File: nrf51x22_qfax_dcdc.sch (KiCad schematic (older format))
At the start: 19 parts, among them U1 nrf51822-qfax, X1 Crystal

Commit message: add vias to footprint and swap in
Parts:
- U1: footprint nrf:nrf51-qfax -> nrf:nrf51-qfax-1ep-vias
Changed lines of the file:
@@
 F 0 "U1" H 2950 4250 60  0000 C CNN
 F 1 "nrf51822-qfax" H 2950 4400 60  0000 C CNN
-F 2 "nrf:nrf51-qfax" H 2900 4650 60  0001 C CNN
+F 2 "nrf:nrf51-qfax-1ep-vias" H 2900 4650 60  0001 C CNN
 F 3 "" H 2900 4650 60  0000 C CNN
 	1    3000 4300

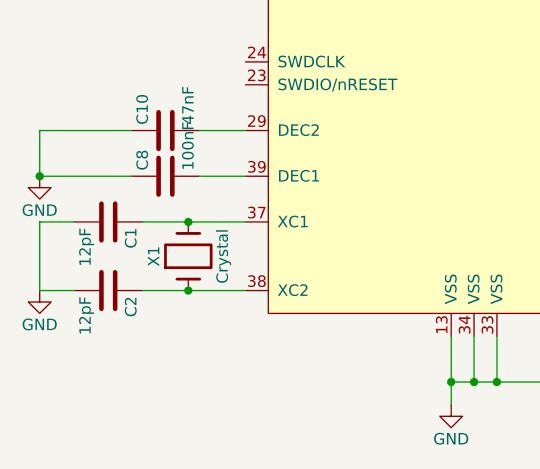
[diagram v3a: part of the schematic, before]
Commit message: fix crystal component so hooks grounds to GND, gerbers
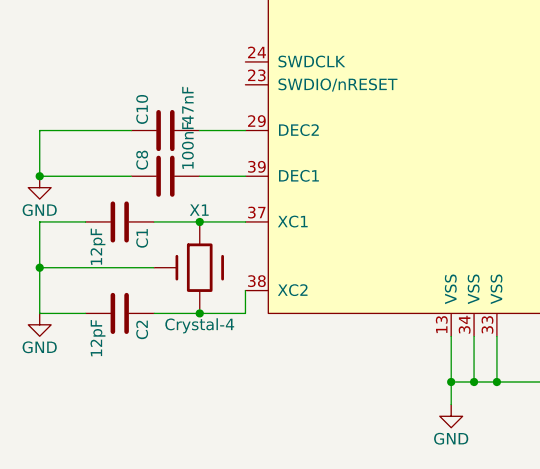
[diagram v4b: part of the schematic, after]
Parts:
- removed X1: Crystal, dcdc:BT-XTAL_2520, symbol Crystal
- added X1: Crystal-4, dcdc:BT-XTAL_2520, symbol Crystal-4
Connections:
- net GND: now also X1.2 (4), X1.4
- net at C2.1, U1.38 (XC2): now also X1.1
- net at C1.1, U1.37 (XC1): now also X1.3
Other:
- moved on the sheet: C1, C2
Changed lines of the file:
@@
 L C C2
 U 1 1 566CD1BB
-P 1200 5800
-F 0 "C2" H 1225 5900 50  0000 L CNN
-F 1 "12pF" H 1225 5700 50  0000 L CNN
-F 2 "dcdc:CAPC1005X04L" H 1238 5650 50  0001 C CNN
-F 3 "" H 1200 5800 50  0000 C CNN
-	1    1200 5800
+P 1250 5900
+F 0 "C2" H 1275 6000 50  0000 L CNN
+F 1 "12pF" H 1275 5800 50  0000 L CNN
+F 2 "dcdc:CAPC1005X04L" H 1288 5750 50  0001 C CNN
+F 3 "" H 1250 5900 50  0000 C CNN
+	1    1250 5900
 	0    1    1    0
 $EndComp
@@
 L C C1
 U 1 1 566CD21B
-P 1200 5500
-F 0 "C1" H 1225 5600 50  0000 L CNN
-F 1 "12pF" H 1225 5400 50  0000 L CNN
-F 2 "dcdc:CAPC1005X04L" H 1238 5350 50  0001 C CNN
-F 3 "" H 1200 5500 50  0000 C CNN
-	1    1200 5500
+P 1250 5500
+F 0 "C1" H 1275 5600 50  0000 L CNN
+F 1 "12pF" H 1275 5400 50  0000 L CNN
+F 2 "dcdc:CAPC1005X04L" H 1288 5350 50  0001 C CNN
+F 3 "" H 1250 5500 50  0000 C CNN
+	1    1250 5500
 	0    1    1    0
 $EndComp
@@
 L GND #PWR05
 U 1 1 566CD572
-P 900 5800
-F 0 "#PWR05" H 900 5550 50  0001 C CNN
-F 1 "GND" H 900 5650 50  0000 C CNN
-F 2 "" H 900 5800 50  0000 C CNN
-F 3 "" H 900 5800 50  0000 C CNN
-	1    900  5800
-	1    0    0    -1
-$EndComp
-Connection ~ 2700 6200
-Wire Wire Line
-	2700 6200 3400 6200
-Connection ~ 2800 6200
-Wire Wire Line
-	1350 5500 1800 5500
-Wire Wire Line
-	1350 5800 1800 5800
-Wire Wire Line
-	4200 2800 5100 2800
-Wire Wire Line
-	3700 2100 3700 2300
-Wire Wire Line
-	3500 2500 3500 2600
-Wire Wire Line
-	3700 2600 3700 2500
-Wire Wire Line
-	3300 2600 3300 2500
-Wire Wire Line
-	3300 2500 3500 2500
-Wire Wire Line
-	3400 1700 3400 2500
-Connection ~ 3400 2500
-Wire Wire Line
-	4400 1700 4400 1900
-Wire Wire Line
-	4100 1700 4100 1900
-Wire Wire Line
-	3400 6200 3400 6000
-Connection ~ 2900 6200
-Connection ~ 1550 5500
-Connection ~ 1550 5800
-Wire Wire Line
-	1050 5800 900  5800
-Wire Wire Line
-	1050 5500 900  5500
-Wire Wire Line
-	900  5500 900  5800
-Wire Wire Line
-	2300 2600 2300 2500
-Wire Wire Line
-	2300 2500 2500 2500
-Wire Wire Line
-	2500 2500 2500 2600
-Wire Wire Line
-	2400 1700 2400 2500
-Connection ~ 2400 2500
-Wire Wire Line
-	2000 2200 2000 2300
-Wire Wire Line
-	2000 2300 2200 2300
-Wire Wire Line
-	4100 2200 4100 2300
-Wire Wire Line
-	4400 2200 4400 2300
+P 900 5900
+F 0 "#PWR05" H 900 5650 50  0001 C CNN
+F 1 "GND" H 900 5750 50  0000 C CNN
+F 2 "" H 900 5900 50  0000 C CNN
+F 3 "" H 900 5900 50  0000 C CNN
+	1    900  5900
+	1    0    0    -1
+$EndComp
 $Comp
 L GND #PWR06
@@
 	1    0    0    -1
 $EndComp
-Wire Wire Line
-	900  5300 1300 5300
-Wire Wire Line
-	900  5100 1300 5100
-Wire Wire Line
-	4800 3000 4800 3100
-Wire Wire Line
-	4800 3300 4800 3400
-Wire Wire Line
-	5400 2800 5800 2800
-Connection ~ 5600 2800
-Wire Wire Line
-	6000 2800 6200 2800
 $Comp
 L GND #PWR07
@@
 	1    0    0    -1
 $EndComp
-Connection ~ 4800 2800
-Wire Wire Line
-	4200 2900 4700 2900
-Wire Wire Line
-	4700 2900 4700 3000
-Wire Wire Line
-	4700 3000 4800 3000
-Wire Wire Line
-	4800 3400 4600 3400
-Wire Wire Line
-	4600 3400 4600 3000
-Wire Wire Line
-	4600 3000 4200 3000
-Connection ~ 4800 3400
-Connection ~ 4800 3000
-Wire Wire Line
-	1800 5100 1600 5100
-Wire Wire Line
-	1800 5300 1600 5300
-Wire Wire Line
-	900  5300 900  5100
-Connection ~ 900  5300
-Connection ~ 4100 1700
-Wire Wire Line
-	3400 1700 4400 1700
-Wire Wire Line
-	2000 1700 2400 1700
-Wire Wire Line
-	2000 1900 2000 1700
-Connection ~ 2000 1700
-Wire Wire Line
-	2200 1900 2200 1700
-Connection ~ 2200 1700
-Wire Wire Line
-	2200 2300 2200 2200
-Connection ~ 2000 2300
-Wire Wire Line
-	3700 1700 3700 1900
-Connection ~ 3700 1700
 Text Label 2000 1600 0    60   ~ 0
 VCC_nRF
-$Comp
-L Crystal X1
-U 1 1 566BCA38
-P 1550 5650
-F 0 "X1" H 1550 5800 50  0000 C CNN
-F 1 "Crystal" H 1550 5500 50  0000 C CNN
-F 2 "dcdc:BT-XTAL_2520" H 1550 5650 50  0001 C CNN
-F 3 "" H 1550 5650 50  0000 C CNN
-	1    1550 5650
-	0    -1   -1   0
-$EndComp
-Wire Wire Line
-	2800 6000 2800 6200
-Wire Wire Line
-	2900 6200 2900 6000
-Wire Wire Line
-	2700 6000 2700 6300
 $Comp
 L nrf51822-qfax U1
@@
 	1    0    0    -1
 $EndComp
+Connection ~ 2700 6200
+Wire Wire Line
+	2700 6200 3400 6200
+Connection ~ 2800 6200
+Wire Wire Line
+	4200 2800 5100 2800
+Wire Wire Line
+	3700 2100 3700 2300
+Wire Wire Line
+	3500 2500 3500 2600
+Wire Wire Line
+	3700 2600 3700 2500
+Wire Wire Line
+	3300 2600 3300 2500
+Wire Wire Line
+	3300 2500 3500 2500
+Wire Wire Line
+	3400 1700 3400 2500
+Connection ~ 3400 2500
+Wire Wire Line
+	4400 1700 4400 1900
+Wire Wire Line
+	4100 1700 4100 1900
+Wire Wire Line
+	3400 6200 3400 6000
+Connection ~ 2900 6200
+Wire Wire Line
+	900  5500 900  5900
+Wire Wire Line
+	2300 2600 2300 2500
+Wire Wire Line
+	2300 2500 2500 2500
+Wire Wire Line
+	2500 2500 2500 2600
+Wire Wire Line
+	2400 1700 2400 2500
+Connection ~ 2400 2500
+Wire Wire Line
+	2000 2200 2000 2300
+Wire Wire Line
+	2000 2300 2200 2300
+Wire Wire Line
+	4100 2200 4100 2300
+Wire Wire Line
+	4400 2200 4400 2300
+Wire Wire Line
+	900  5300 1300 5300
+Wire Wire Line
+	900  5100 1300 5100
+Wire Wire Line
+	4800 3000 4800 3100
+Wire Wire Line
+	4800 3300 4800 3400
+Wire Wire Line
+	5400 2800 5800 2800
+Connection ~ 5600 2800
+Wire Wire Line
+	6000 2800 6200 2800
+Connection ~ 4800 2800
+Wire Wire Line
+	4200 2900 4700 2900
+Wire Wire Line
+	4700 2900 4700 3000
+Wire Wire Line
+	4700 3000 4800 3000
+Wire Wire Line
+	4800 3400 4600 3400
+Wire Wire Line
+	4600 3400 4600 3000
+Wire Wire Line
+	4600 3000 4200 3000
+Connection ~ 4800 3400
+Connection ~ 4800 3000
+Wire Wire Line
+	1800 5100 1600 5100
+Wire Wire Line
+	1800 5300 1600 5300
+Wire Wire Line
+	900  5300 900  5100
+Connection ~ 900  5300
+Connection ~ 4100 1700
+Wire Wire Line
+	3400 1700 4400 1700
+Wire Wire Line
+	2000 1700 2400 1700
+Wire Wire Line
+	2000 1900 2000 1700
+Connection ~ 2000 1700
+Wire Wire Line
+	2200 1900 2200 1700
+Connection ~ 2200 1700
+Wire Wire Line
+	2200 2300 2200 2200
+Connection ~ 2000 2300
+Wire Wire Line
+	3700 1700 3700 1900
+Connection ~ 3700 1700
+Wire Wire Line
+	2800 6000 2800 6200
+Wire Wire Line
+	2900 6200 2900 6000
+Wire Wire Line
+	2700 6000 2700 6300
+Connection ~ 1600 5900
+Wire Wire Line
+	1800 5900 1800 5800
+Wire Wire Line
+	1400 5900 1800 5900
+Wire Wire Line
+	1100 5500 900  5500
+Wire Wire Line
+	900  5900 1100 5900
+Wire Wire Line
+	1400 5700 900  5700
+Connection ~ 900  5700
+Wire Wire Line
+	1400 5500 1800 5500
+Connection ~ 1600 5500
+$Comp
+L Crystal-4 X1
+U 1 1 56D1F3A1
+P 1600 5700
+F 0 "X1" H 1600 5950 50  0000 C CNN
+F 1 "Crystal-4" H 1600 5450 50  0000 C CNN
+F 2 "dcdc:BT-XTAL_2520" H 1600 5700 50  0001 C CNN
+F 3 "" H 1600 5700 50  0000 C CNN
+	1    1600 5700
+	1    0    0    -1
+$EndComp

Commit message: fix missing low freq crystal on schematic
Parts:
- added C13, C14: 12pF, dcdc:CAPC1005X04L, symbol C
- added X2: 32.768kHz, dcdc:XTAL_3215, symbol Crystal_Small
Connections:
- net GND: now also C13.1, C14.1
- net at U1.45 (P0.26): now also C13.2, X2.1
- net at U1.46 (P0.27): now also C14.2, X2.2
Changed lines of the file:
@@
 	1    0    0    -1
 $EndComp
+$Comp
+L C C13
+U 1 1 56D1F8D7
+P 4850 5300
+F 0 "C13" H 4875 5400 50  0000 L CNN
+F 1 "12pF" H 4875 5200 50  0000 L CNN
+F 2 "dcdc:CAPC1005X04L" H 4888 5150 50  0001 C CNN
+F 3 "" H 4850 5300 50  0000 C CNN
+	1    4850 5300
+	0    1    1    0
+$EndComp
+$Comp
+L C C14
+U 1 1 56D1F931
+P 4850 5500
+F 0 "C14" H 4875 5600 50  0000 L CNN
+F 1 "12pF" H 4875 5400 50  0000 L CNN
+F 2 "dcdc:CAPC1005X04L" H 4888 5350 50  0001 C CNN
+F 3 "" H 4850 5500 50  0000 C CNN
+	1    4850 5500
+	0    1    1    0
+$EndComp
+$Comp
+L Crystal_Small X2
+U 1 1 56D1F980
+P 4500 5400
+F 0 "X2" H 4500 5500 50  0000 C CNN
+F 1 "32.768kHz" H 4500 5300 50  0000 C CNN
+F 2 "dcdc:XTAL_3215" H 4500 5400 50  0001 C CNN
+F 3 "" H 4500 5400 50  0000 C CNN
+	1    4500 5400
+	0    1    1    0
+$EndComp
+Wire Wire Line
+	4200 5300 4700 5300
+Connection ~ 4500 5300
+Connection ~ 4500 5500
+Wire Wire Line
+	5000 5500 5100 5500
+Wire Wire Line
+	5100 5300 5100 5600
+Wire Wire Line
+	5100 5300 5000 5300
+$Comp
+L GND #PWR010
+U 1 1 56D20387
+P 5100 5600
+F 0 "#PWR010" H 5100 5350 50  0001 C CNN
+F 1 "GND" H 5100 5450 50  0000 C CNN
+F 2 "" H 5100 5600 50  0000 C CNN
+F 3 "" H 5100 5600 50  0000 C CNN
+	1    5100 5600
+	1    0    0    -1
+$EndComp
+Connection ~ 5100 5500
+Wire Wire Line
+	4200 5400 4300 5400
+Wire Wire Line
+	4300 5400 4300 5500
+Wire Wire Line
+	4300 5500 4700 5500
 $EndSCHEMATC

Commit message: fill in component fields for bom
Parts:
- C1, C13, C14, C2: Description (none) -> Capacitor NP0 ±2%; Distributor 1 (none) -> 490-6197-1-ND; Manufacturer (none) -> Yageo; Manufacturer Part (none) -> GRM1555C1H120GA01D
- C10: Description (none) -> Capacitor X7R ±10%; Distributor 1 (none) -> 311-1717-1-ND; Manufacturer (none) -> Yageo; Manufacturer Part (none) -> CC0402KRX7R8BB473
- C11: Description (none) -> Capacitor X7R ±10%; Distrubutor 1 (none) -> 311-1345-1-ND; Manufacturer (none) -> Yageo; Manufacturer Part (none) -> CC0402KRX7R6BB104
- C12: Description (none) -> Capacitor X7R ±10%; Distributor 1 (none) -> 311-1446-1-ND; Manufacturer (none) -> Yageo; Manufacturer Part (none) -> CC0603KRX7R7BB105
- C3: Description (none) -> Capacitor X7R ±10%; Distributor 1 (none) -> 311-1037-1-ND; Manufacturer (none) -> Yageo; Manufacturer Part (none) -> CC0402KRX7R9BB222
- C4, C5, C6: Description (none) -> Capacitor NP0 ±0.1pF
- C7: Description (none) -> Capacitor X5R ±10%; Distributor 1 (none) -> 490-10730-1-ND; Manufacturer (none) -> Murata Electronics North America; Manufacturer Part (none) -> GRM188R61C475KE11D
- C8: Description (none) -> Capacitor X7R ±10%; Distributor 1 (none) -> 311-1345-1-ND; Manufacturer (none) -> Yageo; Manufacturer Part (none) -> CC0402KRX7R6BB104
- C9: Description (none) -> Capacitor X7R ±10%; Distributor 1 (none) -> 311-1036-1-ND; Manufacturer (none) -> Yageo; Manufacturer Part (none) -> CC0402KRX7R9BB102
- L1, L2, L3: Description (none) -> High frequency chip inductor ±5%
- L4: Description (none) -> Chip inductor IDC min = 50 mA ±20%; Distributor 1 (none) -> 445-6755-1-ND; Manufacturer (none) -> TDK; Manufacturer Part (none) -> MLZ1608N100LT000
- L5: Description (none) -> High frequency chip inductor ±10%; Distributor 1 (none) -> 445-1469-1-ND; Manufacturer (none) -> TDK; Manufacturer Part (none) -> MLK1005S15NJT000
- U1: Manufacturer (none) -> Nordic Semiconductor ASA; Manufacturer Part (none) -> NRF51822-QFAC-T
- X1: Description (none) -> 8pF ±40ppm; Distributor 1 (none) -> 644-1169-1-ND; Manufacturer (none) -> NDK; Manufacturer Part (none) -> NX2520SA-16MHZ-STD-CSW-5
- X2: Description (none) -> 9pF ±20ppm; Distributor 1 (none) -> 535-9544-1-ND; Manufacturer (none) -> Abracon LLC; Manufacturer Part (none) -> ABS07-32.768KHZ-9-T
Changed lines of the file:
@@
 F 2 "dcdc:INDC1005X04L" H 3700 2000 50  0001 C CNN
 F 3 "" H 3700 2000 50  0000 C CNN
+F 4 "High frequency chip inductor ±10%" H 3700 2000 60  0001 C CNN "Description"
+F 5 "MLK1005S15NJT000" H 3700 2000 60  0001 C CNN "Manufacturer Part"
+F 6 "TDK" H 3700 2000 60  0001 C CNN "Manufacturer"
+F 7 "445-1469-1-ND" H 3700 2000 60  0001 C CNN "Distributor 1"
 	1    3700 2000
 	1    0    0    -1
@@
 F 2 "dcdc:INDC1608X06L" H 3700 2400 50  0001 C CNN
 F 3 "" H 3700 2400 50  0000 C CNN
+F 4 "Chip inductor IDC min = 50 mA ±20%" H 3700 2400 60  0001 C CNN "Description"
+F 5 "MLZ1608N100LT000" H 3700 2400 60  0001 C CNN "Manufacturer Part"
+F 6 "TDK" H 3700 2400 60  0001 C CNN "Manufacturer"
+F 7 "445-6755-1-ND" H 3700 2400 60  0001 C CNN "Distributor 1"
 	1    3700 2400
 	1    0    0    -1
@@
 F 2 "dcdc:CAPC1608X06L" H 4438 1900 50  0001 C CNN
 F 3 "" H 4400 2050 50  0000 C CNN
+F 4 "Capacitor X7R ±10%" H 4400 2050 60  0001 C CNN "Description"
+F 5 "CC0603KRX7R7BB105" H 4400 2050 60  0001 C CNN "Manufacturer Part"
+F 6 "Yageo" H 4400 2050 60  0001 C CNN "Manufacturer"
+F 7 "311-1446-1-ND" H 4400 2050 60  0001 C CNN "Distributor 1"
 	1    4400 2050
 	1    0    0    -1
@@
 F 2 "dcdc:CAPC1005X04L" H 4138 1900 50  0001 C CNN
 F 3 "" H 4100 2050 50  0000 C CNN
+F 4 "Capacitor X7R ±10%" H 4100 2050 60  0001 C CNN "Description"
+F 5 "CC0402KRX7R9BB102" H 4100 2050 60  0001 C CNN "Manufacturer Part"
+F 6 "Yageo" H 4100 2050 60  0001 C CNN "Manufacturer"
+F 7 "311-1036-1-ND" H 4100 2050 60  0001 C CNN "Distributor 1"
 	1    4100 2050
 	1    0    0    -1
@@
 F 2 "dcdc:INDC1005X04L" H 4800 3200 50  0001 C CNN
 F 3 "" H 4800 3200 50  0000 C CNN
+F 4 "High frequency chip inductor ±5%" H 4800 3200 60  0001 C CNN "Description"
 	1    4800 3200
 	1    0    0    -1
@@
 F 2 "dcdc:INDC1005X04L" H 4800 2900 50  0001 C CNN
 F 3 "" H 4800 2900 50  0000 C CNN
+F 4 "High frequency chip inductor ±5%" H 4800 2900 60  0001 C CNN "Description"
 	1    4800 2900
 	1    0    0    -1
@@
 F 2 "dcdc:INDC1005X04L" H 5900 2800 50  0001 C CNN
 F 3 "" H 5900 2800 50  0000 C CNN
+F 4 "High frequency chip inductor ±5%" H 5900 2800 60  0001 C CNN "Description"
 	1    5900 2800
 	0    -1   -1   0
@@
 F 2 "dcdc:CAPC1005X04L" H 4838 3400 50  0001 C CNN
 F 3 "" H 4800 3550 50  0000 C CNN
+F 4 "Capacitor X7R ±10%" H 4800 3550 60  0001 C CNN "Description"
+F 5 "CC0402KRX7R9BB222" H 4800 3550 60  0001 C CNN "Manufacturer Part"
+F 6 "Yageo" H 4800 3550 60  0001 C CNN "Manufacturer"
+F 7 "311-1037-1-ND" H 4800 3550 60  0001 C CNN "Distributor 1"
 	1    4800 3550
 	1    0    0    -1
@@
 F 2 "dcdc:CAPC1005X04L" H 1488 5150 50  0001 C CNN
 F 3 "" H 1450 5300 50  0000 C CNN
+F 4 "Capacitor X7R ±10%" H 1450 5300 60  0001 C CNN "Description"
+F 5 "CC0402KRX7R6BB104" H 1450 5300 60  0001 C CNN "Manufacturer Part"
+F 6 "Yageo" H 1450 5300 60  0001 C CNN "Manufacturer"
+F 7 "311-1345-1-ND" H 1450 5300 60  0001 C CNN "Distributor 1"
 	1    1450 5300
 	0    -1   -1   0
@@
 F 2 "dcdc:CAPC1005X04L" H 1488 4950 50  0001 C CNN
 F 3 "" H 1450 5100 50  0000 C CNN
+F 4 "Capacitor X7R ±10%" H 1450 5100 60  0001 C CNN "Description"
+F 5 "CC0402KRX7R8BB473" H 1450 5100 60  0001 C CNN "Manufacturer Part"
+F 6 "Yageo" H 1450 5100 60  0001 C CNN "Manufacturer"
+F 7 "311-1717-1-ND" H 1450 5100 60  0001 C CNN "Distributor 1"
 	1    1450 5100
 	0    -1   -1   0
@@
 F 2 "dcdc:CAPC1608X06L" H 2038 1900 50  0001 C CNN
 F 3 "" H 2000 2050 50  0000 C CNN
+F 4 "Capacitor X5R ±10%" H 2000 2050 60  0001 C CNN "Description"
+F 5 "GRM188R61C475KE11D" H 2000 2050 60  0001 C CNN "Manufacturer Part"
+F 6 "Murata Electronics North America" H 2000 2050 60  0001 C CNN "Manufacturer"
+F 7 "490-10730-1-ND" H 2000 2050 60  0001 C CNN "Distributor 1"
 	1    2000 2050
 	1    0    0    -1
@@
 F 2 "dcdc:CAPC1005X04L" H 2238 1900 50  0001 C CNN
 F 3 "" H 2200 2050 50  0000 C CNN
+F 4 "Capacitor X7R ±10%" H 2200 2050 60  0001 C CNN "Description"
+F 5 "CC0402KRX7R6BB104" H 2200 2050 60  0001 C CNN "Manufacturer Part"
+F 6 "Yageo" H 2200 2050 60  0001 C CNN "Manufacturer"
+F 7 "311-1345-1-ND" H 2200 2050 60  0001 C CNN "Distrubutor 1"
 	1    2200 2050
 	1    0    0    -1
@@
 F 2 "dcdc:CAPC1005X04L" H 5288 2650 50  0001 C CNN
 F 3 "" H 5250 2800 50  0000 C CNN
+F 4 "Capacitor NP0 ±0.1pF" H 5250 2800 60  0001 C CNN "Description"
 	1    5250 2800
 	0    1    1    0
@@
 F 2 "dcdc:CAPC1005X04L" H 5638 2800 50  0001 C CNN
 F 3 "" H 5600 2950 50  0000 C CNN
+F 4 "Capacitor NP0 ±0.1pF" H 5600 2950 60  0001 C CNN "Description"
 	1    5600 2950
 	1    0    0    -1
@@
 F 2 "dcdc:CAPC1005X04L" H 6238 2800 50  0001 C CNN
 F 3 "" H 6200 2950 50  0000 C CNN
+F 4 "Capacitor NP0 ±0.1pF" H 6200 2950 60  0001 C CNN "Description"
 	1    6200 2950
 	1    0    0    -1
@@
 F 2 "dcdc:CAPC1005X04L" H 1288 5750 50  0001 C CNN
 F 3 "" H 1250 5900 50  0000 C CNN
+F 4 "Capacitor NP0 ±2%" H 1250 5900 60  0001 C CNN "Description"
+F 5 "GRM1555C1H120GA01D" H 1250 5900 60  0001 C CNN "Manufacturer Part"
+F 6 "Yageo" H 1250 5900 60  0001 C CNN "Manufacturer"
+F 7 "490-6197-1-ND" H 1250 5900 60  0001 C CNN "Distributor 1"
 	1    1250 5900
 	0    1    1    0
@@
 F 2 "dcdc:CAPC1005X04L" H 1288 5350 50  0001 C CNN
 F 3 "" H 1250 5500 50  0000 C CNN
+F 4 "Capacitor NP0 ±2%" H 1250 5500 60  0001 C CNN "Description"
+F 5 "GRM1555C1H120GA01D" H 1250 5500 60  0001 C CNN "Manufacturer Part"
+F 6 "Yageo" H 1250 5500 60  0001 C CNN "Manufacturer"
+F 7 "490-6197-1-ND" H 1250 5500 60  0001 C CNN "Distributor 1"
 	1    1250 5500
 	0    1    1    0
@@
 F 2 "nrf:nrf51-qfax-1ep-vias" H 2900 4650 60  0001 C CNN
 F 3 "" H 2900 4650 60  0000 C CNN
+F 4 "NRF51822-QFAC-T" H 3000 4300 60  0001 C CNN "Manufacturer Part"
+F 5 "Nordic Semiconductor ASA" H 3000 4300 60  0001 C CNN "Manufacturer"
 	1    3000 4300
 	1    0    0    -1
@@
 F 2 "dcdc:BT-XTAL_2520" H 1600 5700 50  0001 C CNN
 F 3 "" H 1600 5700 50  0000 C CNN
+F 4 "8pF ±40ppm" H 1600 5700 60  0001 C CNN "Description"
+F 5 "NX2520SA-16MHZ-STD-CSW-5" H 1600 5700 60  0001 C CNN "Manufacturer Part"
+F 6 "NDK" H 1600 5700 60  0001 C CNN "Manufacturer"
+F 7 "644-1169-1-ND" H 1600 5700 60  0001 C CNN "Distributor 1"
 	1    1600 5700
 	1    0    0    -1
@@
 F 2 "dcdc:CAPC1005X04L" H 4888 5150 50  0001 C CNN
 F 3 "" H 4850 5300 50  0000 C CNN
+F 4 "Capacitor NP0 ±2%" H 4850 5300 60  0001 C CNN "Description"
+F 5 "GRM1555C1H120GA01D" H 4850 5300 60  0001 C CNN "Manufacturer Part"
+F 6 "Yageo" H 4850 5300 60  0001 C CNN "Manufacturer"
+F 7 "490-6197-1-ND" H 4850 5300 60  0001 C CNN "Distributor 1"
 	1    4850 5300
 	0    1    1    0
@@
 F 2 "dcdc:CAPC1005X04L" H 4888 5350 50  0001 C CNN
 F 3 "" H 4850 5500 50  0000 C CNN
+F 4 "Capacitor NP0 ±2%" H 4850 5500 60  0001 C CNN "Description"
+F 5 "GRM1555C1H120GA01D" H 4850 5500 60  0001 C CNN "Manufacturer Part"
+F 6 "Yageo" H 4850 5500 60  0001 C CNN "Manufacturer"
+F 7 "490-6197-1-ND" H 4850 5500 60  0001 C CNN "Distributor 1"
 	1    4850 5500
 	0    1    1    0
@@
 F 2 "dcdc:XTAL_3215" H 4500 5400 50  0001 C CNN
 F 3 "" H 4500 5400 50  0000 C CNN
+F 4 "9pF ±20ppm" H 4500 5400 60  0001 C CNN "Description"
+F 5 "ABS07-32.768KHZ-9-T" H 4500 5400 60  0001 C CNN "Manufacturer Part"
+F 6 "Abracon LLC" H 4500 5400 60  0001 C CNN "Manufacturer"
+F 7 "535-9544-1-ND" H 4500 5400 60  0001 C CNN "Distributor 1"
 	1    4500 5400
 	0    1    1    0
